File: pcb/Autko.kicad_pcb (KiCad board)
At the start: 4 copper layers, 140 x 155 mm, 130 parts, among them J1 PDI, M1 LEFT, M2 RIGHT, Q1 Si4368DY, SW1 POWER, SW2 START, SW3 STOP, U1 LTC3872, U10 CNY70, U11 TB6612FNG, U12 74HC2G14, U13 74HC2G14, U14 RN4678, U2 uA78M33, U3 ATxmega16A4U-A, U4 CNY70, U5 CNY70, U6 CNY70, U7 CNY70, U8 CNY70, U9 CNY70, X1 8MHz

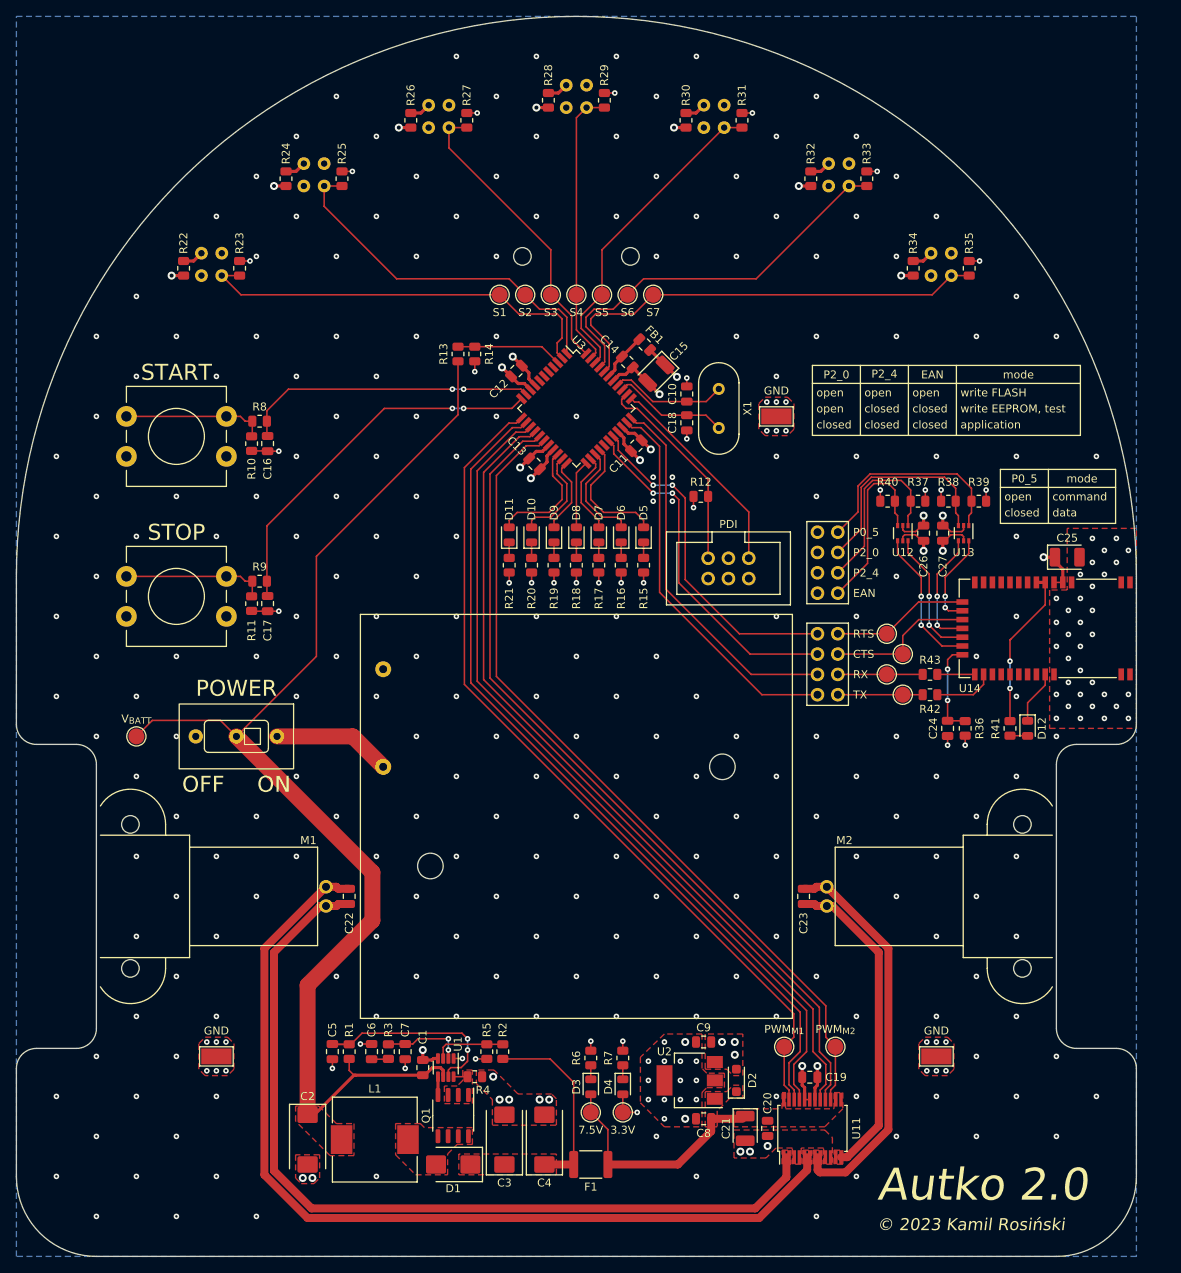
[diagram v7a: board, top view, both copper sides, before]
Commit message: [pcb] Inductor upgrade, boost converter clean-up
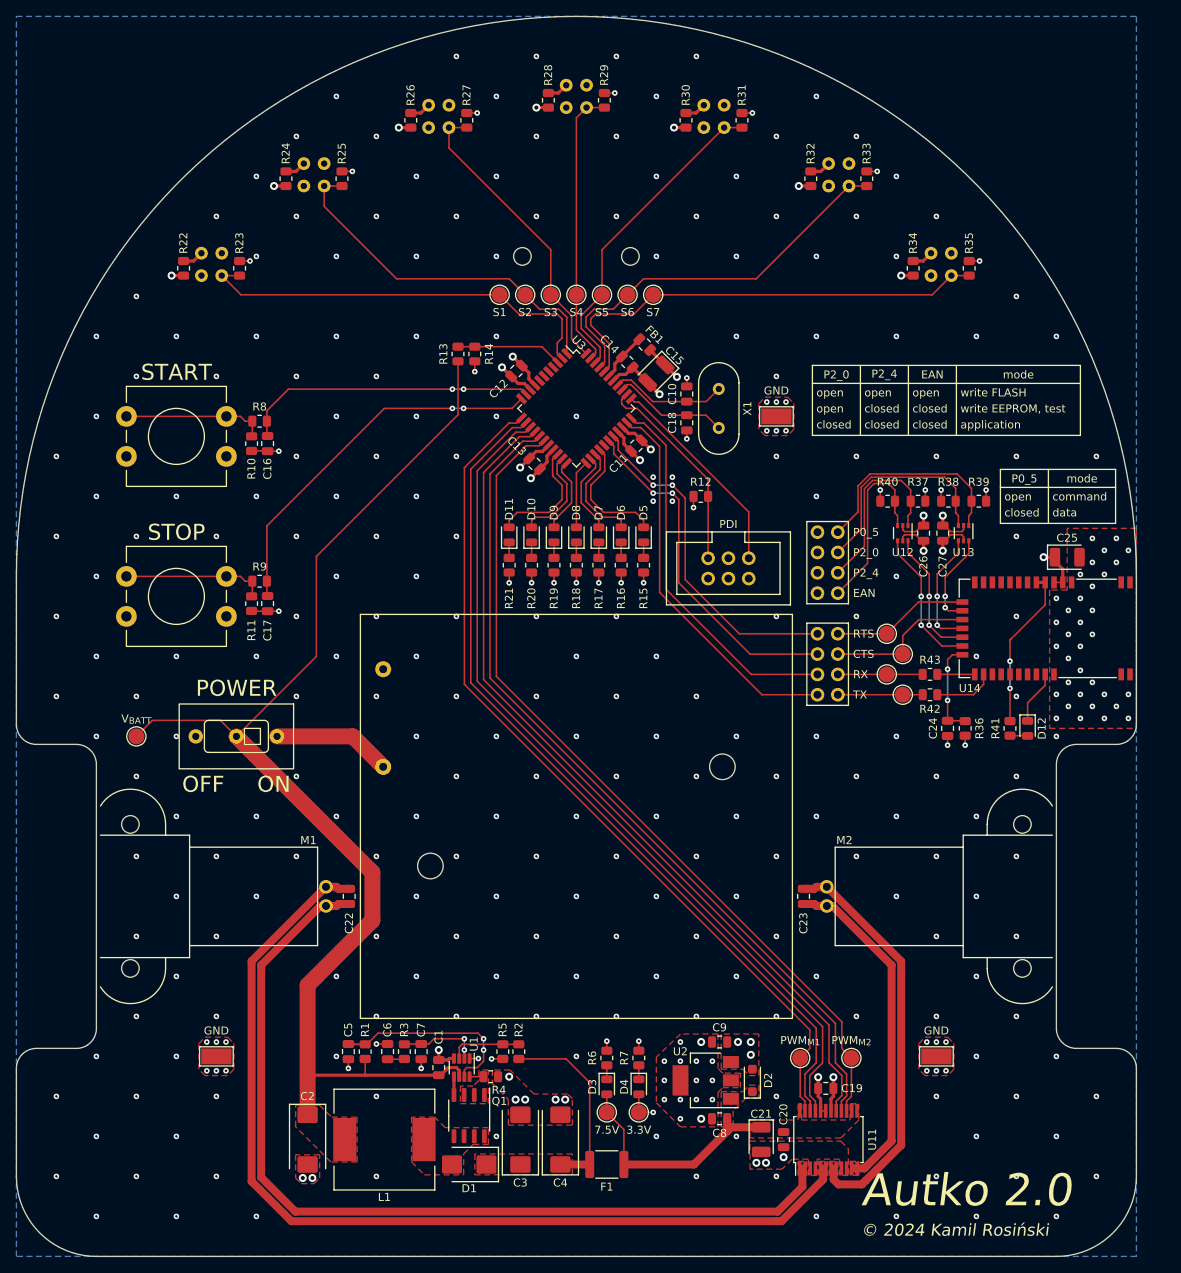
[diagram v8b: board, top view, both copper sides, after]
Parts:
- D1: value SKL34 -> SL52-3G
- L1: footprint Inductor_SMD:L_10.4x10.4_H4.8 -> Inductor_SMD:L_12x12mm_H6mm
- Q1: value Si4368DY -> ~
- moved C19 2.44 mm to (130.7, 164.5)
- moved C20 2.44 mm to (125.4, 170.9)
- moved C21 2.44 mm to (122.6, 170.9)
- moved U11 2.44 mm to (131.0, 170.9)
- moved TP14 2.44 mm to (127.5, 160.7)
- moved TP15 2.44 mm to (133.9, 160.7)
- moved C1 2.00 mm to (82.3, 161.9)
- moved C3 2.00 mm to (92.5, 170.9)
- moved C4 2.00 mm to (97.5, 170.9)
- moved C5 2.00 mm to (71.0, 159.9)
- moved C6 2.00 mm to (75.9, 159.9)
- moved C7 2.00 mm to (80.1, 159.9)
- moved C8 2.00 mm to (117.4, 168.3)
- moved C9 2.00 mm to (117.4, 158.7)
- moved D1 2.00 mm to (86.1, 174.0)
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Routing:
- net Net-(M1--): track 116.7 -> 121.1 mm
- net Net-(M1-+): track 109.7 -> 114.1 mm
- net Net-(M2-+): track 40.3 -> 42.6 mm
- net /Microcontroller/M1_PWM: track 106.5 -> 108.7 mm
- net /Microcontroller/M1_IN2: track 106.0 -> 108.3 mm
- net /Microcontroller/M2_PWM: track 103.6 -> 105.8 mm
- net /Microcontroller/M1_IN1: track 105.5 -> 107.8 mm
- net /Microcontroller/M2_IN2: track 104.3 -> 106.5 mm
- net /Microcontroller/M2_IN1: track 105.0 -> 107.2 mm
- net Net-(M2--): track 49.7 -> 51.6 mm
- net +BATT: track 152.8 -> 152.3 mm
- net +7.5V: track 29.8 -> 30.3 mm
- net GND: vias 333 -> 342
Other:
- board text added: "© 2024 Kamil Rosiński"
- board text removed: "© 2023 Kamil Rosiński"
